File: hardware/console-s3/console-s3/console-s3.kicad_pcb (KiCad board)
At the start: 2 copper layers, 64 x 22.9 mm, 46 parts, among them J1 USB-C, J2 PANEL, Q1 S8050, Q2 AO3401A, SW1 D0, SW2 D1, SW3 D2, SW4 PREV, SW5 BACK, U1 ESP32-S3-WROOM-1-N4R2, U2 ATECC608C, U3 ME6211C33, U4 USBLC6-2SC6

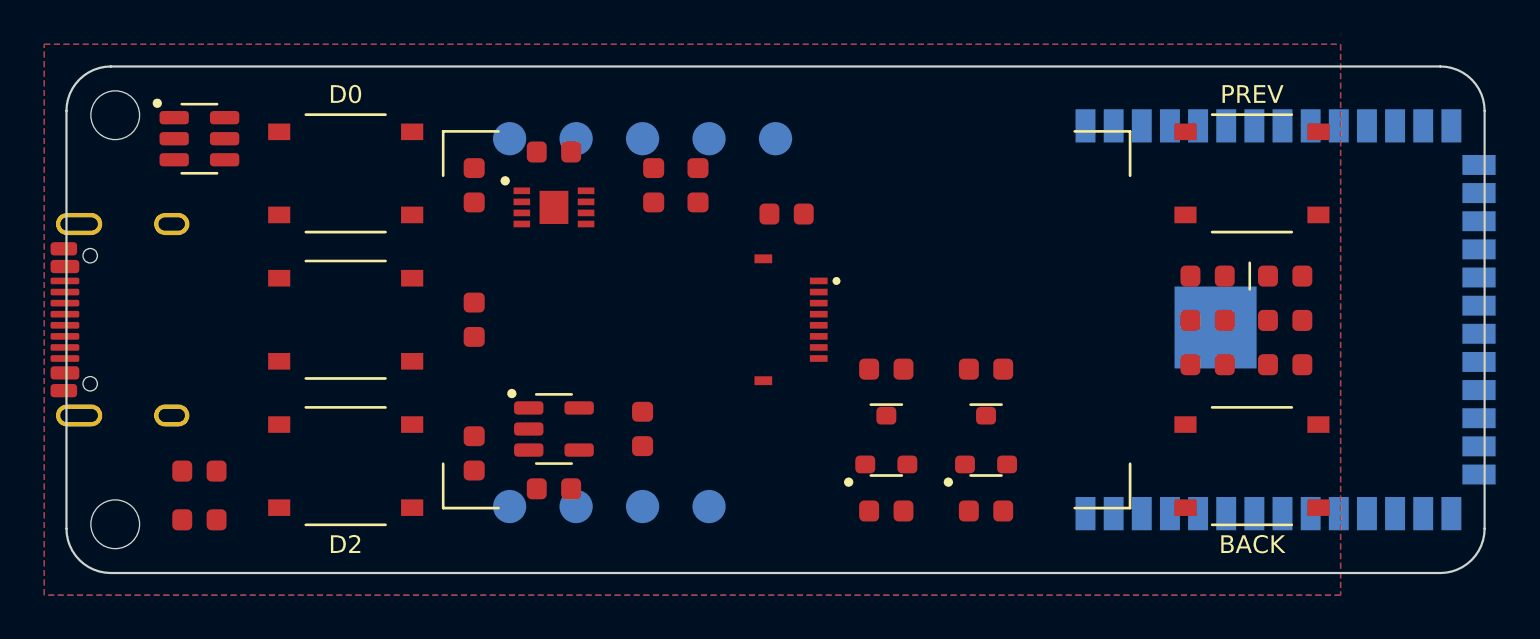
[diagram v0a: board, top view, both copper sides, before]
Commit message: console-s3: routed with Freerouting, brand silkscreen, BOOT and RESET
tools/keypcb route console-s3 routes the placed board with Freerouting
2.5 through KiCad's Specctra files, then drops dangling vias, stitches
ground and fills. The generator writes the board placed, plus locked
escape tracks for J1's USB pads and U2's bus. 537 tracks, 1066 mm, 70
vias (19 stitching).

- C5 turned toward U2; U4 moved; USB split at U4 (USB_DP/DN on J1's
  side, S3_DP/DN on the module's); 2.5 mm no-track rings round H1/H2.
- The silkscreen: the name traced from Atkinson Hyperlegible Next Bold
  (wordmark.py), the logos, and under the glass an 8-bit key below U2
  with a dragon guarding it, after Adventure (Atari 2600).
- The two right-hand buttons are BOOT (GPIO0, beside D0) and RESET (EN
  to ground) in place of PREV and BACK. The image never read those.
- Text 1.0 mm with 0.15 strokes; the project rules raised to match.

console-pocket's rotate(), which this generator shares, is fixed as on
claude/wing-a-refine (the same change on both branches).

KiCad 10.0.6, tools/keypcb check console-s3: ERC 0/0, DRC 0, 0
unconnected, 0 parity issues. Fab files in console-s3/fab/. Not ordered.
No firmware change.

Co-Authored-By: Claude Opus 5.5 <noreply@anthropic.com>
Claude-Session: https://claude.ai/code/session_014mGuGD4x9Si2dmdRKbhRec
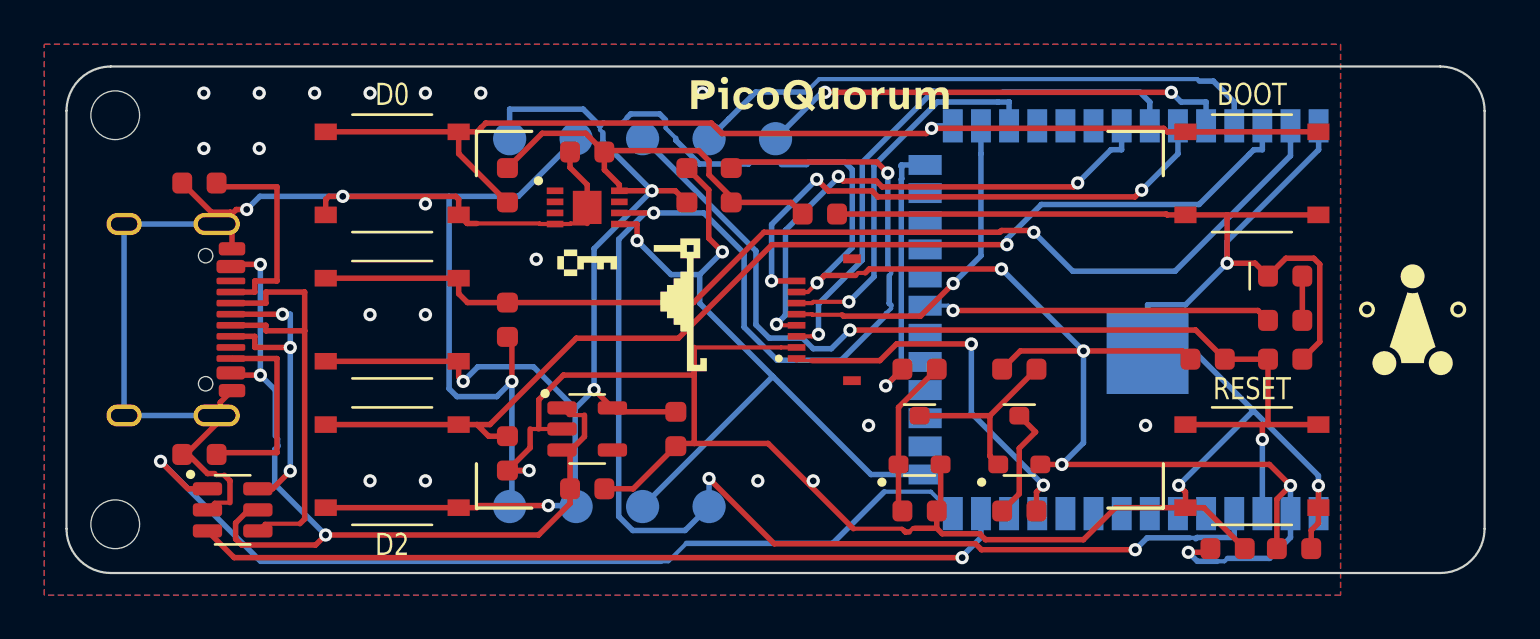
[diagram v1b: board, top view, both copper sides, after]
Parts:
- removed LOGO1: PicoQuorum_Mark, picoquorum:PicoQuorum_Mark
- SW4: value PREV -> BOOT
- SW5: value BACK -> RESET
- moved U4 16.8 mm to (107.5, 137.2)
- moved R10 13.0 mm to (106.0, 122.4), turned to 180 degrees
- moved C3 12.3 mm to (152.4, 138.9)
- moved C4 11.0 mm to (155.4, 138.9)
- moved R11 2.95 mm to (106.0, 134.7), turned to 180 degrees
- moved SW1 2.10 mm to (114.7, 122.0)
- moved SW2 2.10 mm to (114.7, 128.6)
- moved SW3 2.10 mm to (114.7, 135.2)
- moved C1 1.50 mm to (123.5, 136.2)
- moved C2 1.50 mm to (127.5, 133.5), turned to -90 degrees
- moved C5 1.50 mm to (123.5, 121.0), turned to 180 degrees
- moved C6 1.50 mm to (134.0, 123.8)
- moved J2 1.50 mm to (134.2, 128.6), turned to 90 degrees
- moved Q1 1.50 mm to (138.5, 134.0)
- moved Q2 1.50 mm to (143.0, 134.0)
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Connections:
- SW4 pad 1: /BTN_PREV -> /BTN_D0
- SW5 pad 1: /BTN_BACK -> /EN
- U1 pad 13: /USB_DN -> /S3_DN
- U1 pad 14: /USB_DP -> /S3_DP
- U1 pad 5: /BTN_PREV -> unconnected-(U1-IO5-Pad5)
- U1 pad 6: /BTN_BACK -> unconnected-(U1-IO6-Pad6)
- U4 pad 1: /USB_DP -> /S3_DP
- U4 pad 3: /USB_DN -> /S3_DN
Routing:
- net GND: track 0.00 -> 212.2 mm, vias 0 -> 26
- net +3V3: track 0.00 -> 146.9 mm, vias 0 -> 10
- net /SCL: track 0.00 -> 78.6 mm, vias 0 -> 4
- net /BTN_D0: track 0.00 -> 50.4 mm, vias 0 -> 1
- net /BTN_D2: track 0.00 -> 50.2 mm, vias 0 -> 1
- net /BTN_D1: track 0.00 -> 50.0 mm, vias 0 -> 1
- net /EN: track 0.00 -> 48.0 mm, vias 0 -> 2
- net /S3_DP: track 0.00 -> 42.0 mm, vias 0 -> 1
- net VBUS: track 0.00 -> 40.1 mm, vias 0 -> 3
- net /S3_DN: track 0.00 -> 36.9 mm, vias 0 -> 1
- net /SDA: track 0.00 -> 33.9 mm, vias 0 -> 2
- net /TXD0: track 0.00 -> 26.3 mm
- net /LCD_CS: track 0.00 -> 25.3 mm, vias 0 -> 3
- net /LCD_RST: track 0.00 -> 25.2 mm, vias 0 -> 1
- net /LCD_DC: track 0.00 -> 23.5 mm, vias 0 -> 3
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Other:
- board text added: "BOOT"
- board text added: "Nothing signs unseen"
- board text added: "RESET"
- board text added: "console-s3 rev A · CERN-OHL-W 2.0"
- board text removed: "BACK"
- board text removed: "CERN-OHL-W 2.0"
- board text removed: "PREV"
- board text removed: "PicoQuorum console-s3 A"

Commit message: console-s3: J1's slot rings 0.25, R8 clear of the fold, U3's heat path; the order plan
The three things tools/keypcb jlc pointed to, then routed again:
- J1's shell pads 0.1 mm bigger, so its plated slots' rings are 0.25 mm,
  not JLCPCB's bare 0.20. The slots are the same.
- R8 upright at (52.2, 10.4), 0.7 mm clear of the panel ribbon's guessed
  fold instead of under it.
- U3's ground pin solid to the pour, with a track to a via under its
  body into the back pour.
504 tracks, 1051 mm, 74 vias (17 stitching).

The back's Source Location reads PicoQuorum.app, whose home page links
to the source.

ORDER-PLAN-2026-10-24.md: what to select at JLCPCB for five boards, and
the choice it turns on. Every ESP32-S3-WROOM-1 is Standard-only there,
so Economic assembly (recommended, about $75 less) fits the front and
the module goes on by hand; Standard fits both sides but needs a panel.
A second board to be decided.

The self-test's golden-picture case now thins a track: a via added
inside its own net's copper on both faces draws no different.

KiCad 10.0.6: tools/keypcb check console-s3 ERC 0/0, DRC 0, 0
unconnected, 0 parity; gen_console_s3.py --check clean; tools/keypcb
jlc console-s3 every check passes (U3's heat still a warning); the
self-test 10 of 10.

Co-Authored-By: Claude Opus 5.5 <noreply@anthropic.com>
Claude-Session: https://claude.ai/code/session_014mGuGD4x9Si2dmdRKbhRec
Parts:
- moved R8 1.03 mm to (152.2, 129.6), turned to -90 degrees
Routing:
- net /BTN_D2: track 50.2 -> 74.8 mm, vias 1 -> 3
- net /SCL: track 78.6 -> 56.7 mm, vias 4 -> 2
- net +3V3: track 146.9 -> 134.1 mm
- net /LCD_CS: track 25.3 -> 20.9 mm, vias 3 -> 1
- net /LCD_RST: track 25.2 -> 29.5 mm
- net GND: track 212.2 -> 208.5 mm, vias 26 -> 25
- net /BTN_D1: track 50.0 -> 53.4 mm, vias 1 -> 3
- net VBUS: track 40.1 -> 37.9 mm, vias 3 -> 4
- net /LCD_BL: track 12.4 -> 10.4 mm
- net /S3_DP: track 42.0 -> 40.1 mm, vias 1 -> 3
- net /LCD_MOSI: track 15.3 -> 17.2 mm
- net /EN: track 48.0 -> 46.2 mm, vias 2 -> 4
- net /LCD_LEDA: track 17.3 -> 18.3 mm
- net /LCD_DC: track 23.5 -> 24.2 mm, vias 3 -> 1
- net /BL_D: track 5.23 -> 4.62 mm
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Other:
- board text added: "PicoQuorum.app"
- board text removed: "github.com/jmcpheron/pico-quorum"

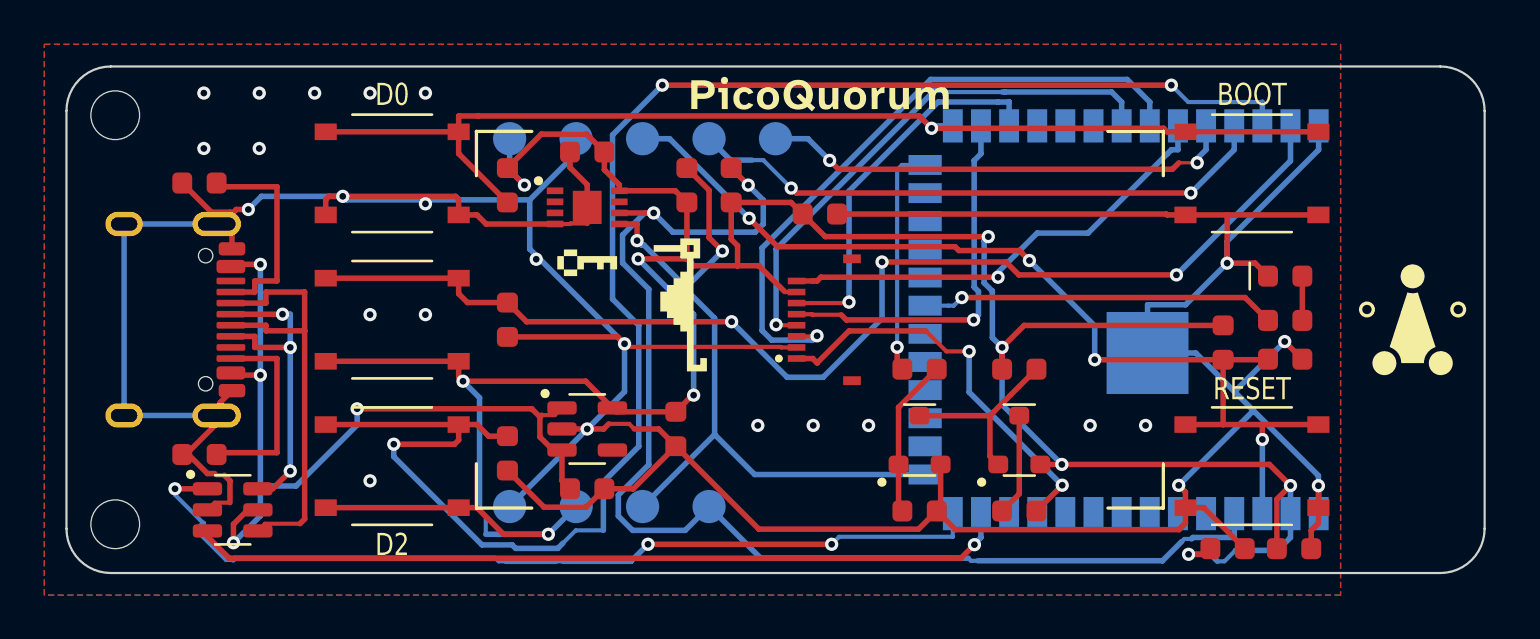
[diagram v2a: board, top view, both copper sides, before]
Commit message: console-s3: backlight from VBUS, longer module pads, J2 at the 21 mm reach
- The backlight was likely over-driven: 10 R from 3.3 V gave 20-40 mA against the
  panel's 20 mA maximum (ER-TFT1.14-2). It now runs from VBUS through 150 R
  (C22808): (5 - 3.0) V / 150 R = 13 mA, 16 mA at worst. Q2 and R4 move to VBUS.
- The module's pads reached 0.45 mm past its edge; they now reach 1.45 mm, as on
  PicoQuorumKey, for the iron. The courtyard and pin-1 dot follow.
- J2 moves to x 30.0, for the datasheet's folded reach of 21.0 +/- 0.5 mm from the
  glass's edge (it was 4.7 mm shorter). C6, the key and dragon art move with it, and
  the 3D fit models the fold from the same drawing.
- Placed, routed and checked again: ERC 0, DRC 0, parity 0; tools/keypcb jlc
  passes, its self-test 10/10; golden images rewritten.
- DESIGN.md drops the stale "No reset button" note: BOOT and RESET are on the board.

Co-Authored-By: Claude Opus 5.5 <noreply@anthropic.com>
Claude-Session: https://claude.ai/code/session_014mGuGD4x9Si2dmdRKbhRec
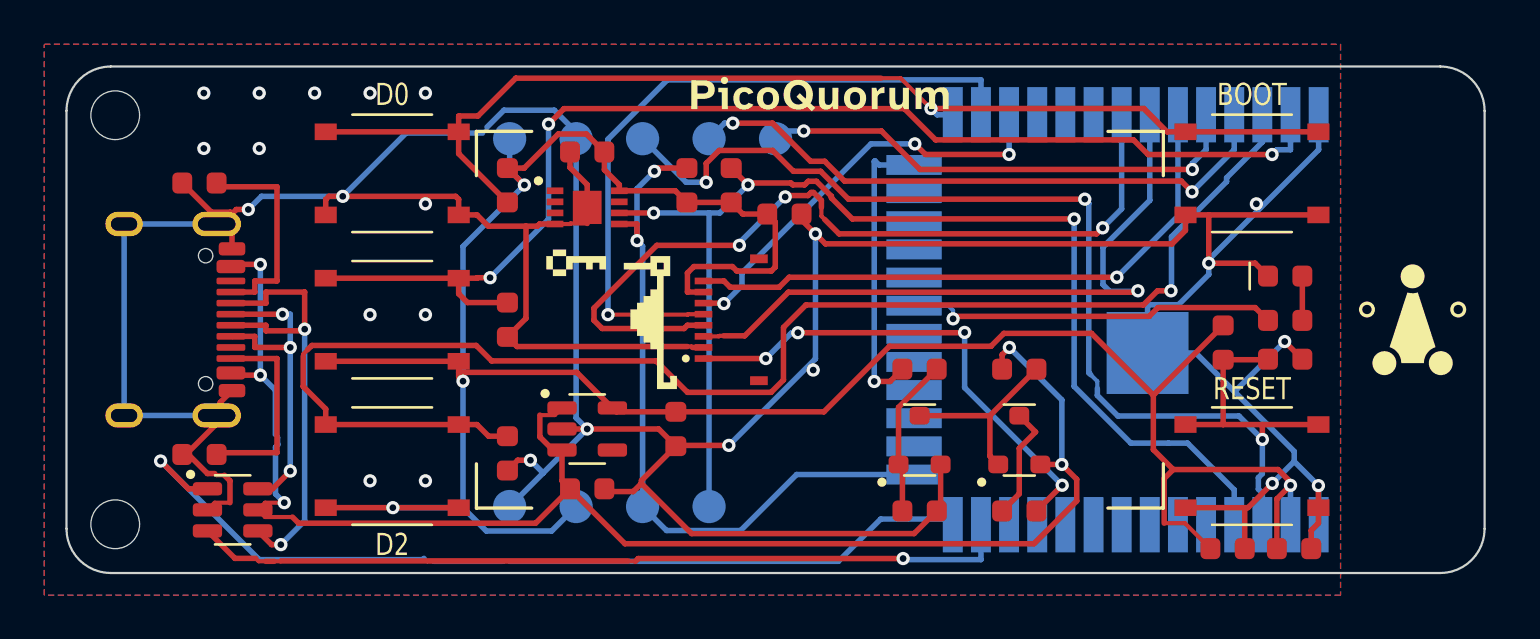
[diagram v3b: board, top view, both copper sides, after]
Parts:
- R1: value 10R -> 150R
- moved J2 4.20 mm to (130.0, 128.6)
- moved C6 1.60 mm to (132.4, 123.8)
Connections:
- Q2 pad 2: +3V3 -> VBUS
- R4 pad 1: +3V3 -> VBUS
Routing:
- net VBUS: track 37.9 -> 70.6 mm, vias 4 -> 5
- net /LCD_MOSI: track 17.2 -> 31.8 mm
- net /LCD_DC: track 24.2 -> 37.7 mm, vias 1 -> 3
- net +3V3: track 134.1 -> 122.8 mm, vias 10 -> 4
- net /BTN_D2: track 74.8 -> 65.2 mm, vias 3 -> 1
- net /EN: track 46.2 -> 55.8 mm, vias 4 -> 3
- net /LCD_CS: track 20.9 -> 27.4 mm
- net GND: track 208.5 -> 213.0 mm, vias 25 -> 24
- net /LCD_LEDA: track 18.3 -> 22.6 mm, vias 2 -> 4
- net /LCD_BL: track 10.4 -> 13.3 mm
- net /SCL: track 56.7 -> 54.5 mm, vias 2 -> 3
- net /LCD_SCK: track 17.4 -> 19.1 mm, vias 1 -> 3
- net /BTN_D0: track 50.9 -> 52.4 mm
- net /BTN_D1: track 53.4 -> 54.8 mm
- net /LCD_RST: track 29.5 -> 30.7 mm
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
